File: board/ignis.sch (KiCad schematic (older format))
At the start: 10 parts, among them U1 PIC18F13K22

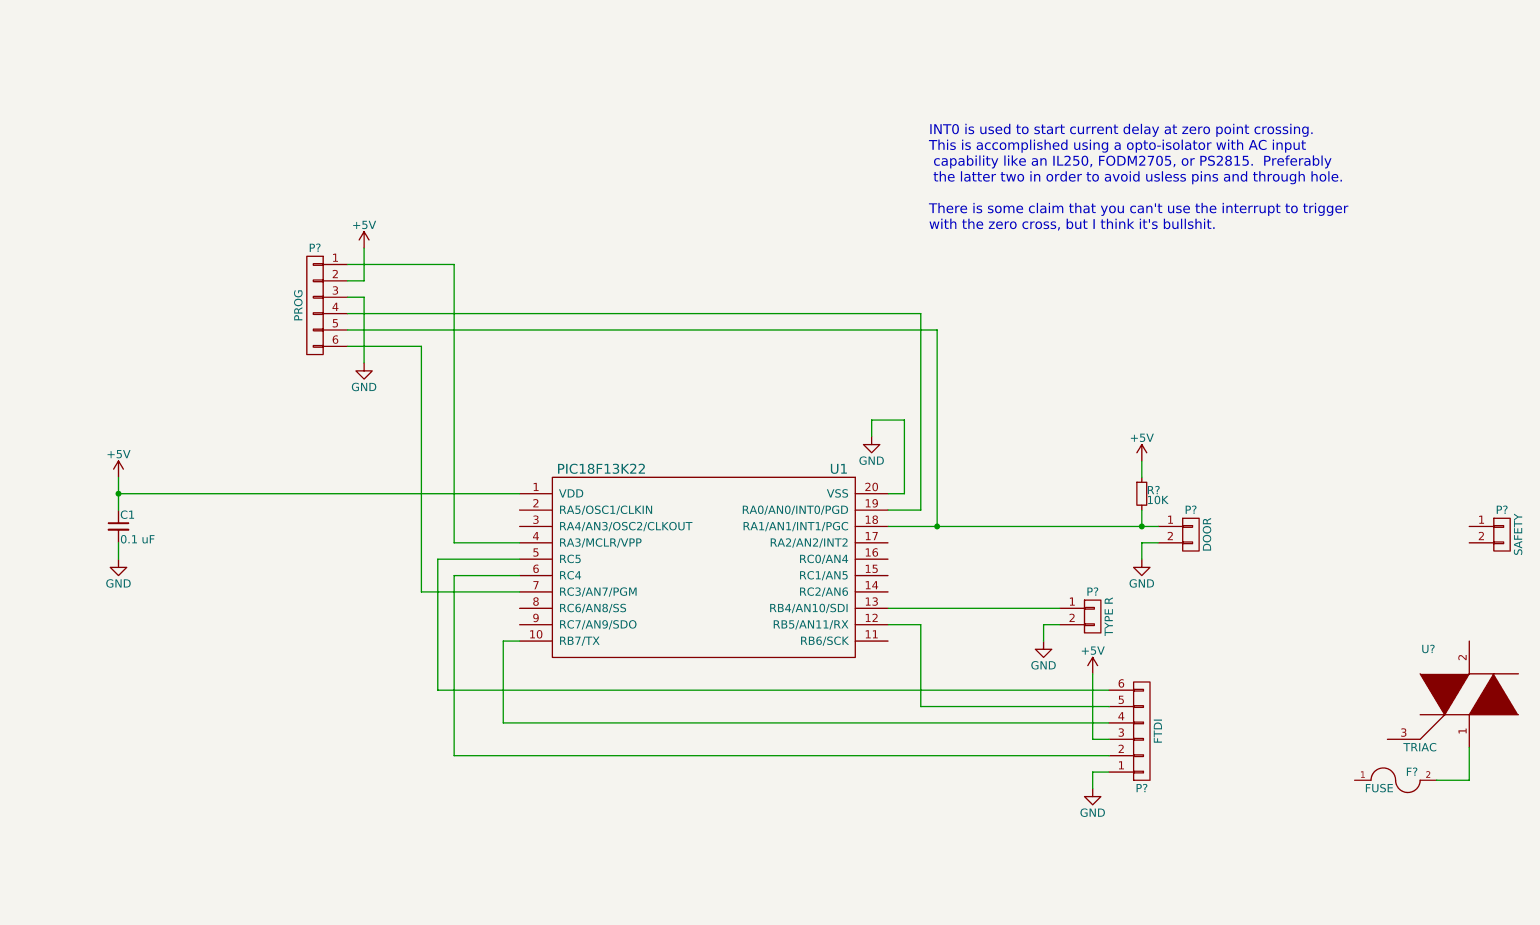
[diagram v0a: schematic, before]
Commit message: Revised insulation plan.
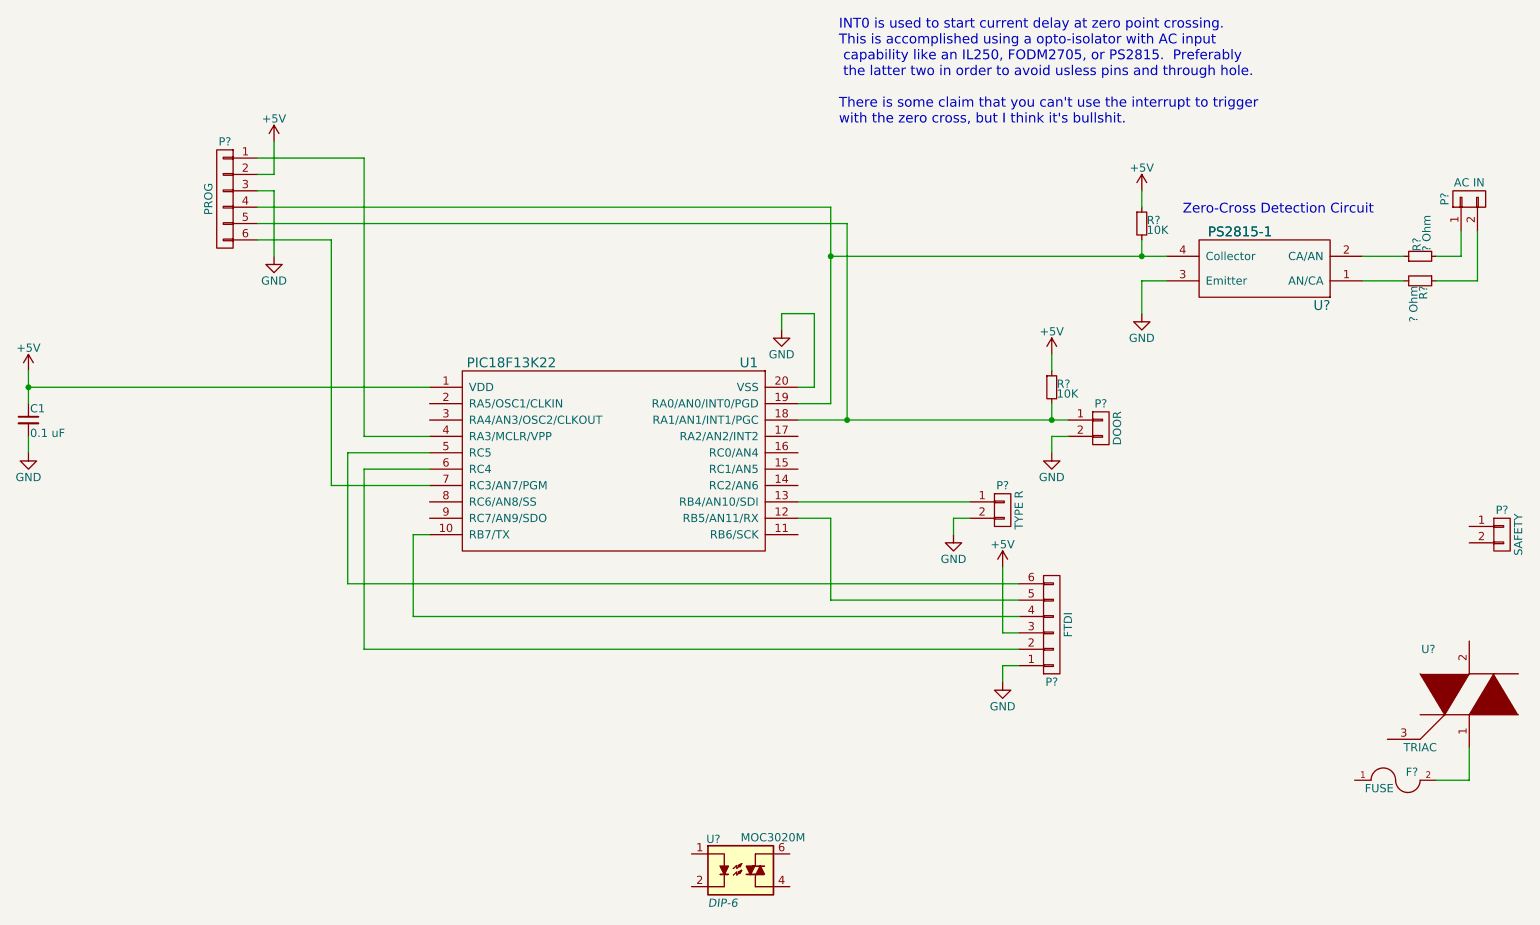
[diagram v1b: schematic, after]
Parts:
- added P?: AC IN, symbol CONN_01X02
- added R? (x2): ? Ohm, symbol R_Small
- added R?: 10K, symbol R_Small
- added U?: PS2815-1, ugw:PS2815-1, symbol PS2815-1
- added U?: MOC3020M, DIP-6, symbol MOC3020M
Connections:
- net +5V: now also R?.1
- net GND: now also U?.3 (Emitter)
- net at P?.4 (P4), U1.19 (RA0/AN0/INT0/PGD): now also R?.2, U?.4 (Collector)
- new net: P?.1 (P1), R?.2
- new net: P?.2 (P2), R?.1
- new net: R?.2, U?.1 (AN/CA)
- new net: R?.1, U?.2 (CA/AN)
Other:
- note added: "Zero-Cross Detection Circuit"
- moved on the sheet: C1, P?, R?, U1

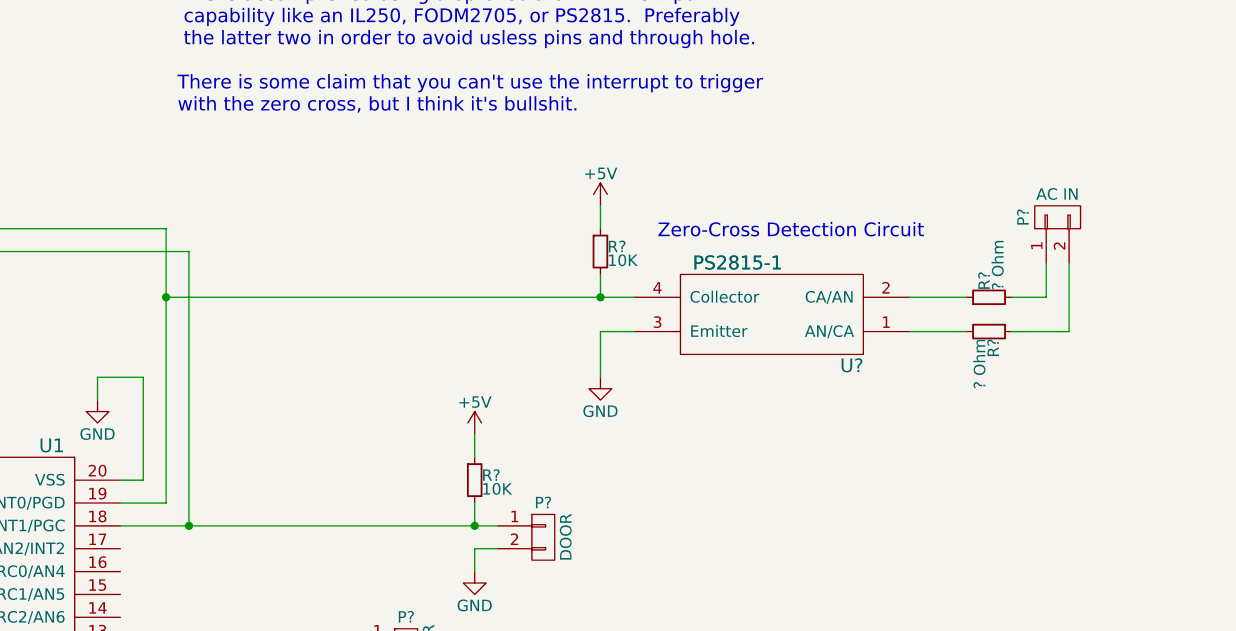
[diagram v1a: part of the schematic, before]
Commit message: Finalized the Zero-Cross circuit via experimentation.
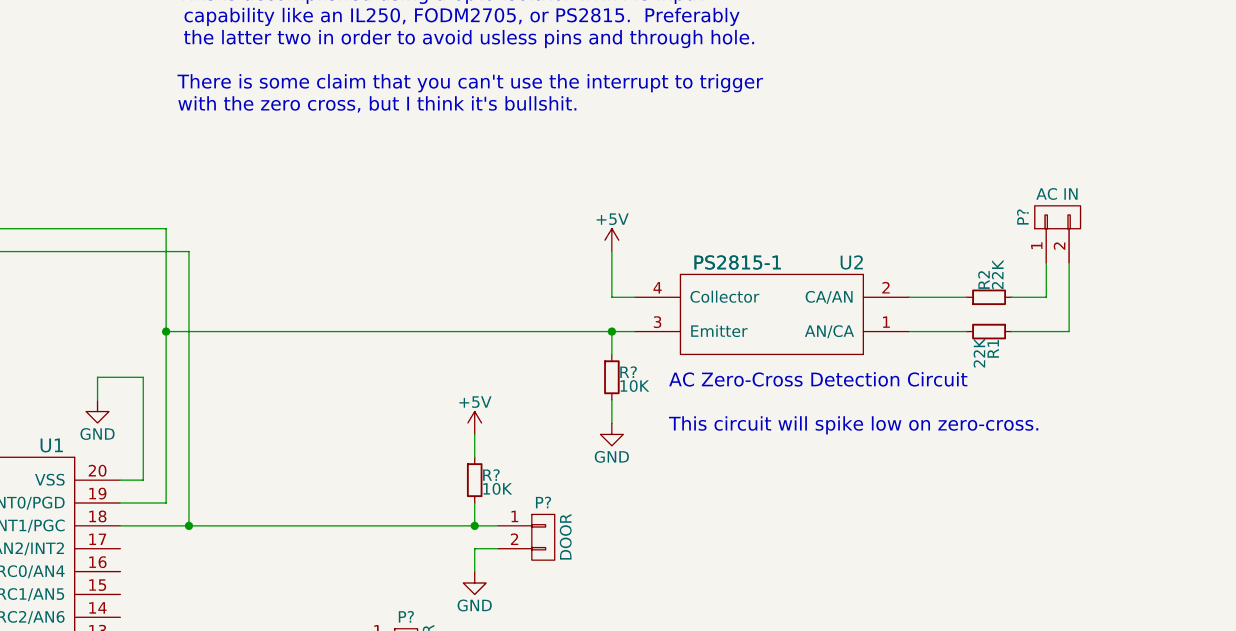
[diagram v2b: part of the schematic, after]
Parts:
- R1, R2: renamed from R?; value ? Ohm -> 22K
- gave numbers to parts that had none: 1
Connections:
- net +5V: now also U2.4 (Collector); no longer R?.1
- net GND: now also R?.2; no longer U2.3 (Emitter)
- net at P?.4 (P4), U1.19 (RA0/AN0/INT0/PGD): now also R?.1, U2.3 (Emitter); no longer R?.2, U2.4 (Collector)
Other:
- note added: "AC Zero-Cross Detection Circuit\n\nThis circuit will spike low on zero-cross."
- note removed: "Zero-Cross Detection Circuit"
- moved on the sheet: R?
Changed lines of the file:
@@
 $EndComp
 Connection ~ 6000 3050
-Connection ~ 5900 2050
 $Comp
 L CONN_01X02 P?
@@
 $EndComp
 $Comp
-L PS2815-1 U?
+L PS2815-1 U2
 U 1 1 578F1611
 P 8550 2150
-F 0 "U?" H 8200 2350 60  0000 C CNN
+F 0 "U2" H 8200 1900 60  0000 C CNN
 F 1 "PS2815-1" H 8700 1900 60  0000 C CNN
 F 2 "ugw:PS2815-1" H 8600 1900 60  0001 C CNN
@@
 $EndComp
 $Comp
-L R_Small R?
+L R_Small R1
 U 1 1 578F1617
 P 9500 2200
-F 0 "R?" H 9530 2220 50  0000 L CNN
-F 1 "? Ohm" H 9530 2160 50  0000 L CNN
+F 0 "R1" H 9530 2220 50  0000 L CNN
+F 1 "22K" H 9530 2160 50  0000 L CNN
 F 2 "" H 9500 2200 50  0000 C CNN
 F 3 "" H 9500 2200 50  0000 C CNN
@@
 $EndComp
 $Comp
-L R_Small R?
+L R_Small R2
 U 1 1 578F161D
 P 9500 2050
-F 0 "R?" H 9530 2070 50  0000 L CNN
-F 1 "? Ohm" H 9530 2010 50  0000 L CNN
+F 0 "R2" H 9530 2070 50  0000 L CNN
+F 1 "22K" H 9530 2010 50  0000 L CNN
 F 2 "" H 9500 2050 50  0000 C CNN
 F 3 "" H 9500 2050 50  0000 C CNN
@@
 L GND #PWR?
 U 1 1 578F1629
-P 7800 2400
-F 0 "#PWR?" H 7800 2150 50  0001 C CNN
-F 1 "GND" H 7800 2250 50  0000 C CNN
-F 2 "" H 7800 2400 50  0000 C CNN
-F 3 "" H 7800 2400 50  0000 C CNN
-	1    7800 2400
+P 7850 2600
+F 0 "#PWR?" H 7850 2350 50  0001 C CNN
+F 1 "GND" H 7850 2450 50  0000 C CNN
+F 2 "" H 7850 2600 50  0000 C CNN
+F 3 "" H 7850 2600 50  0000 C CNN
+	1    7850 2600
 	1    0    0    -1
 $EndComp
-Wire Wire Line
-	7800 2200 7950 2200
 $Comp
 L +5V #PWR?
 U 1 1 578F1631
-P 7800 1650
-F 0 "#PWR?" H 7800 1500 50  0001 C CNN
-F 1 "+5V" H 7800 1790 50  0000 C CNN
-F 2 "" H 7800 1650 50  0000 C CNN
-F 3 "" H 7800 1650 50  0000 C CNN
-	1    7800 1650
+P 7850 1850
+F 0 "#PWR?" H 7850 1700 50  0001 C CNN
+F 1 "+5V" H 7850 1990 50  0000 C CNN
+F 2 "" H 7850 1850 50  0000 C CNN
+F 3 "" H 7850 1850 50  0000 C CNN
+	1    7850 1850
 	1    0    0    -1
 $EndComp
-Connection ~ 7800 2050
-Wire Wire Line
-	7800 1950 7800 2050
 $Comp
 L MOC3020M U?
@@
 	1    0    0    -1
 $EndComp
-Text Notes 8050 1800 0    60   ~ 0
-Zero-Cross Detection Circuit
-Wire Wire Line
-	7800 2400 7800 2200
-Wire Wire Line
-	5900 2050 7950 2050
-Wire Wire Line
-	7800 1650 7800 1750
 $Comp
 L R_Small R?
 U 1 1 578F1637
-P 7800 1850
-F 0 "R?" H 7830 1870 50  0000 L CNN
-F 1 "10K" H 7830 1810 50  0000 L CNN
-F 2 "" H 7800 1850 50  0000 C CNN
-F 3 "" H 7800 1850 50  0000 C CNN
-	1    7800 1850
+P 7850 2400
+F 0 "R?" H 7880 2420 50  0000 L CNN
+F 1 "10K" H 7880 2360 50  0000 L CNN
+F 2 "" H 7850 2400 50  0000 C CNN
+F 3 "" H 7850 2400 50  0000 C CNN
+	1    7850 2400
 	1    0    0    -1
 $EndComp
@@
 Wire Wire Line
 	9850 2200 9600 2200
+Wire Wire Line
+	5900 2200 7950 2200
+Wire Wire Line
+	7850 2200 7850 2300
+Wire Wire Line
+	7850 2600 7850 2500
+Wire Wire Line
+	7850 1850 7850 2050
+Connection ~ 5900 2200
+Connection ~ 7850 2200
+Wire Wire Line
+	7850 2050 7950 2050
+Text Notes 8100 2650 0    60   ~ 0
+AC Zero-Cross Detection Circuit\n\nThis circuit will spike low on zero-cross.
 $EndSCHEMATC

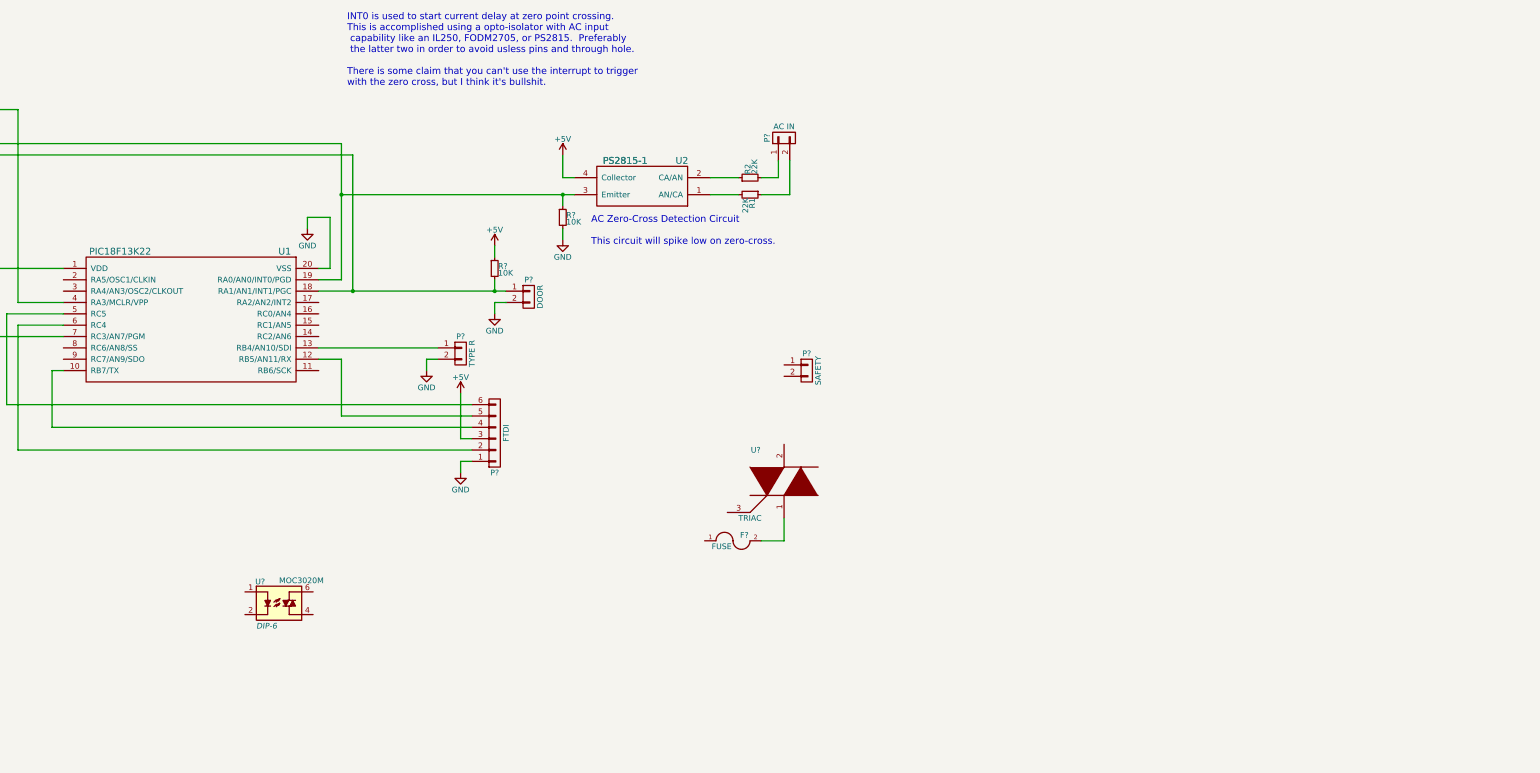
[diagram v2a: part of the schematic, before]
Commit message: TRIAC control circuit.
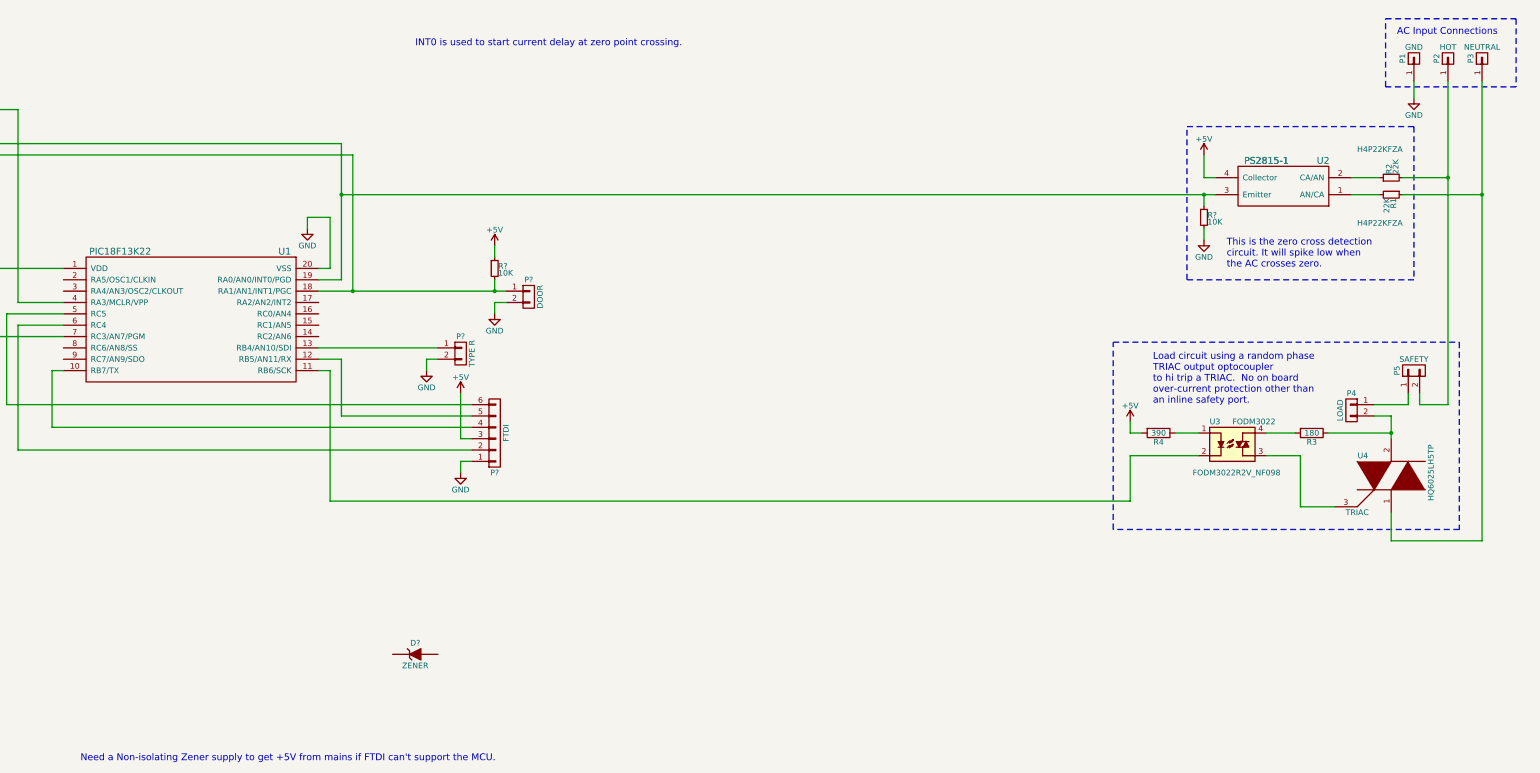
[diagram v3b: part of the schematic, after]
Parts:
- removed F?: FUSE, symbol FUSE
- removed P?: AC IN, symbol CONN_01X02
- removed U?: MOC3020M, DIP-6, symbol MOC3020M
- added D?: ZENER, symbol ZENER
- added P1: GND, symbol CONN_01X01
- added P2: HOT, symbol CONN_01X01
- added P3: NEUTRAL, symbol CONN_01X01
- added P4: LOAD, symbol CONN_01X02
- added R3: 180, symbol R
- added R4: 390, symbol R
- added U3: FODM3022, MFP4L, symbol FODM3022
- gave numbers to parts that had none: 2
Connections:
- net +5V: now also R4.2
- net GND: now also P1.1 (P1)
- net at U4.1: now also R1.1, P3.1 (P1)
- net at U4.2: now also P4.2 (P2), R3.1
- net at U4.3: now also U3.3
- net at U1.11 (RB6/SCK): now also U3.2
- net at P5.1 (P1): now also P4.1 (P1)
- net at P5.2 (P2): now also R2.2, P2.1 (P1)
- new net: R4.1, U3.1
- new net: R3.2, U3.4
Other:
- note added: "AC Input Connections"
- note added: "INT0 is used to start current delay at zero point crossing."
- note added: "Load circuit using a random phase \nTRIAC output optocoupler\nto hi trip a TRIAC. No on board\nover-current protection other than \nan inline safety port."
- note added: "Need a Non-isolating Zener supply to get +5V from mains if FTDI can't support the MCU."
- note added: "This is the zero cross detection \ncircuit. It will spike low when \nthe AC crosses zero."
- note removed: "AC Zero-Cross Detection Circuit\n\nThis circuit will spike low on zero-cross."
- note removed: "INT0 is used to start current delay at zero point crossing.\nThis is accomplished using a opto-isolator with AC input\n capability like an IL250, FODM2705, or PS2815. Preferably\n the latter two in order to avoid usless pins and through hole.\n\nThere is some claim that you can't use the interrupt to trigger\nwith the zero cross, but I think it's bullshit."
- moved on the sheet: P5, R1, R2, R?, U2, U4
